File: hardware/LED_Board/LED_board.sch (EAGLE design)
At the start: 116 parts, among them U1 IS31FL3731-SALS2, U5 MSL0402RGBU1

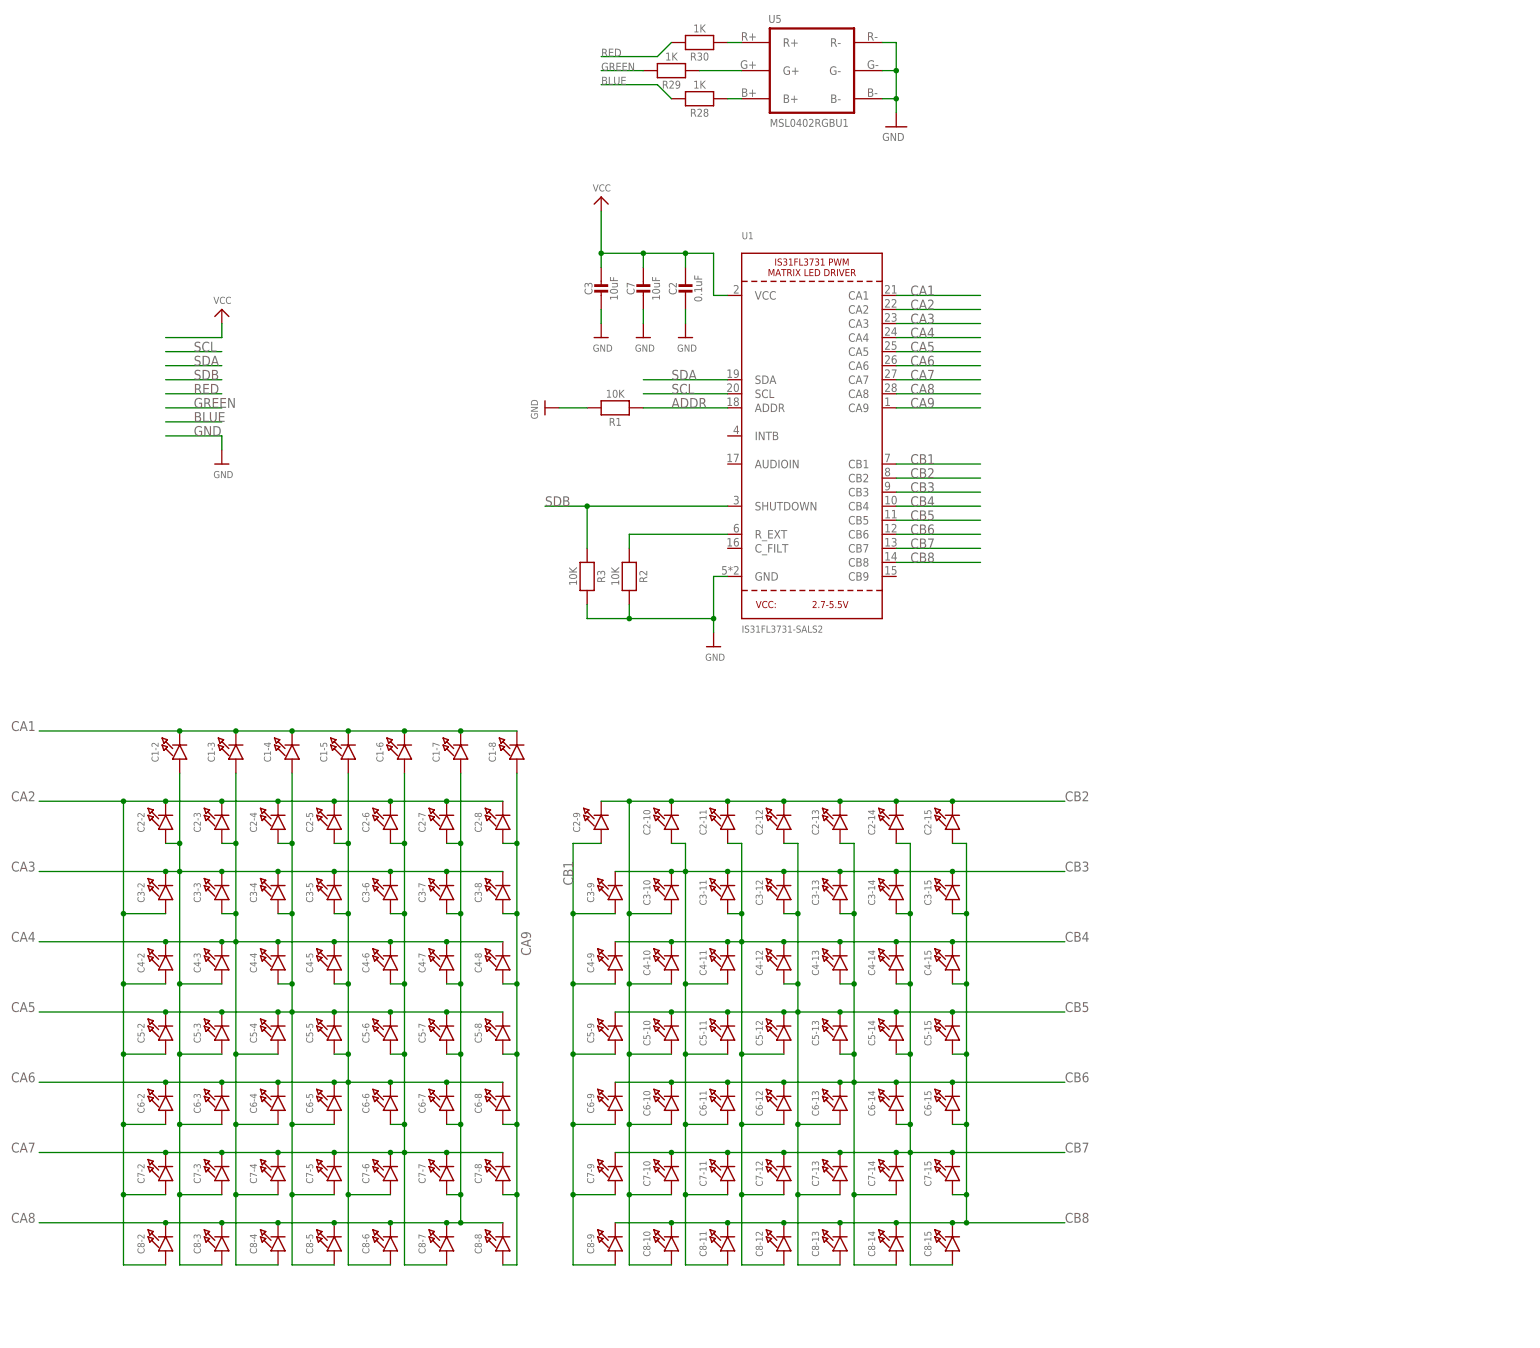
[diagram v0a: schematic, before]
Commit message: Merged control board and power board, updated LED board
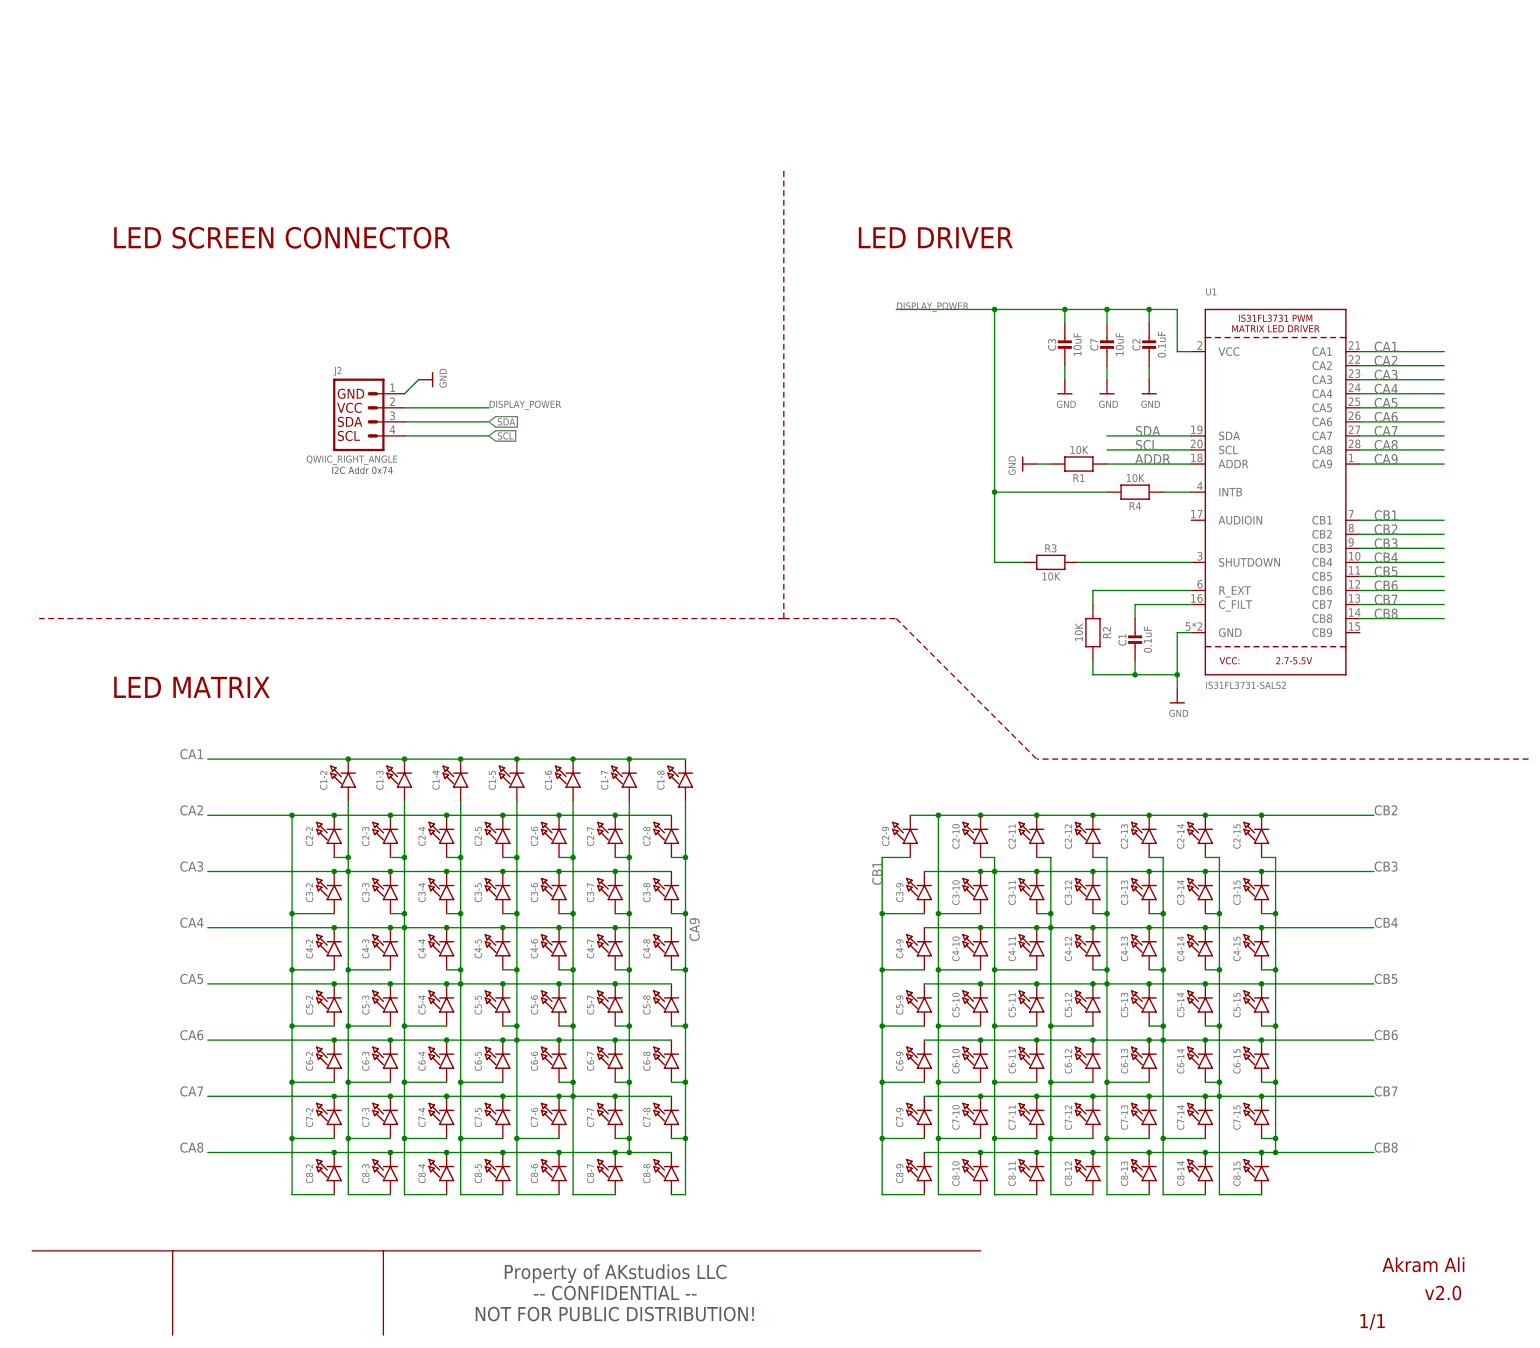
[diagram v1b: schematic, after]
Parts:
- removed R28, R29, R30: 1K, Adafruit Feather 32u4 Bluefruit LE:MICROBUILDER_RESISTOR_0402MP
- removed U5: MSL0402RGBU1, MSL0402RGBU1:MSL0402RGBU1
- added C1: 0.1uF, Adafruit Feather 32u4 Bluefruit LE:MICROBUILDER_CAP_CERAMIC_0402MP
- added J2: QWIIC_RIGHT_ANGLE, SparkFun-Connectors:QWIIC_CONNECTORJS-1MM
- added R4: 10K, Adafruit Feather 32u4 Bluefruit LE:MICROBUILDER_RESISTOR_0402MP
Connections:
- removed net BLUE: R28.2
- removed net GREEN: R29.2
- removed net N$16: R28.1, U5.B+
- removed net N$18: R30.1, U5.R+
- removed net N$24: R29.1, U5.G+
- removed net RED: R30.2
- removed net SDB: R3.1, U1.SHUTDOWN
- removed net VCC: C2.1, C3.1, C7.1, U1.VCC
- new net DISPLAY_POWER: C2.1, C3.1, C7.1, J2.2, R3.1, R4.2, U1.VCC
- new net N$1: R3.2, U1.SHUTDOWN
- new net N$2: C1.1, U1.C_FILT
- new net N$3: R4.1, U1.INTB
- net GND: now also C1.2, J2.1; no longer R3.2, U5.B-, U5.G-, U5.R-
- net SCL: now also J2.4
- net SDA: now also J2.3
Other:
- note added: "-- CONFIDENTIAL -- NOT FOR PUBLIC DISTRIBUTION!"
- note added: "Akram Ali"
- note added: "I2C Addr 0x74"
- note added: "LED DRIVER"
- note added: "LED MATRIX"
- note added: "LED SCREEN CONNECTOR"
- note added: "Property of AKstudios LLC"
- note added: "v2.0"
- moved on the sheet: C1-2, C1-3, C1-4, C1-5, C1-6, C1-7, C1-8, C2, C2-10, C2-11, C2-12, C2-13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
